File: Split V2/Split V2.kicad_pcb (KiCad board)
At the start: 2 copper layers, 170.2 x 121.3 mm, 75 parts, among them J1 AudioJack4

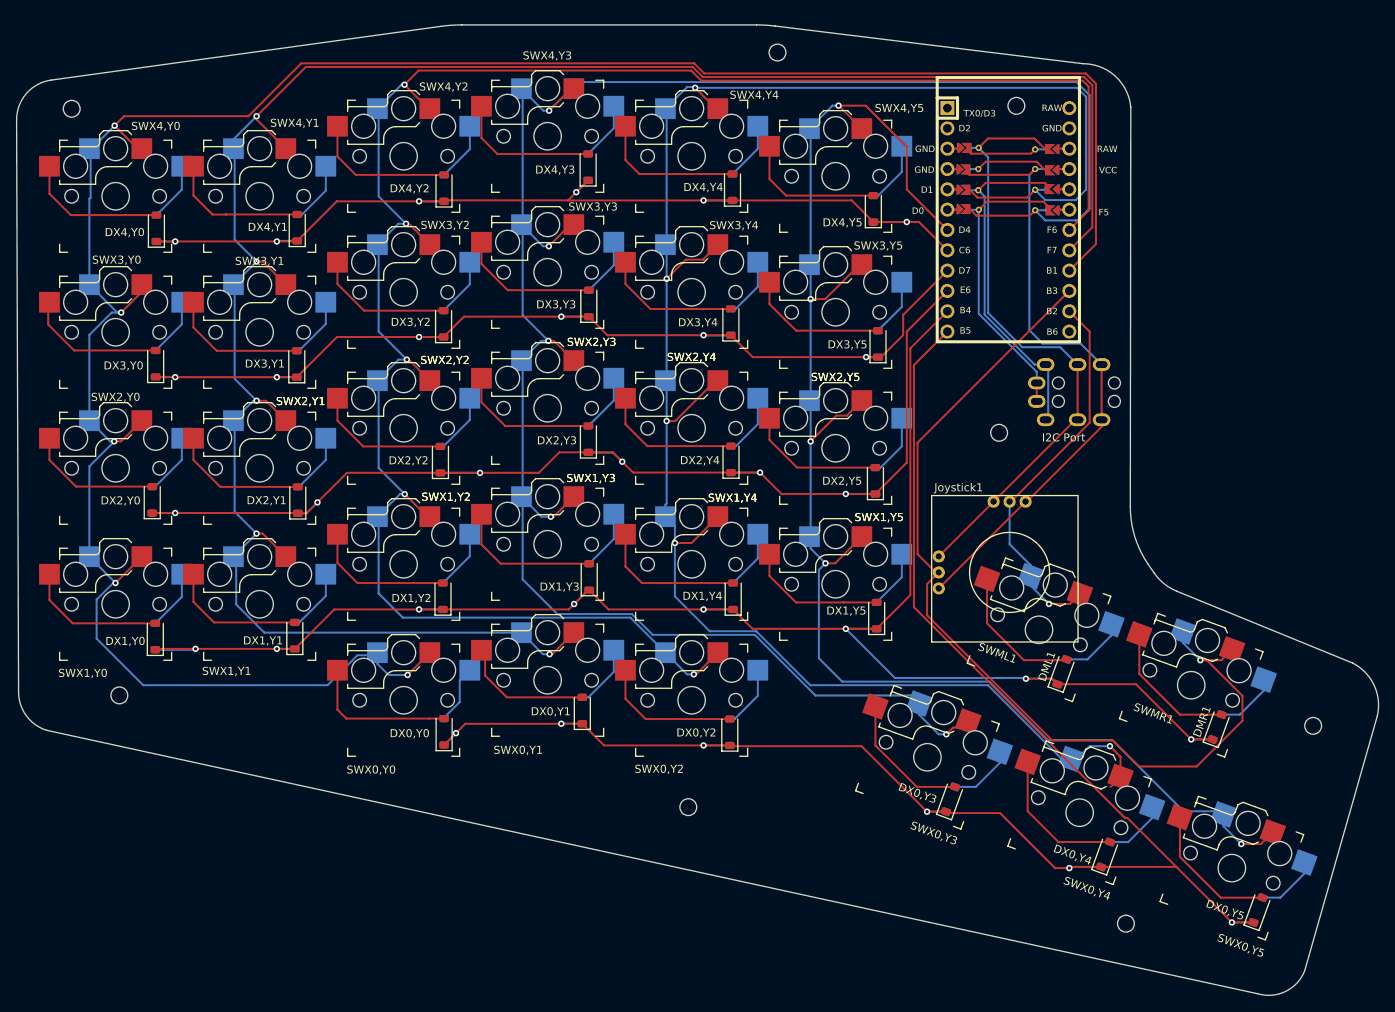
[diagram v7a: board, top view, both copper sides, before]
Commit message: Modified Split and made new
Modified the original split to correct ADC error for joystick and started work on a Split keyboard with cherry switches
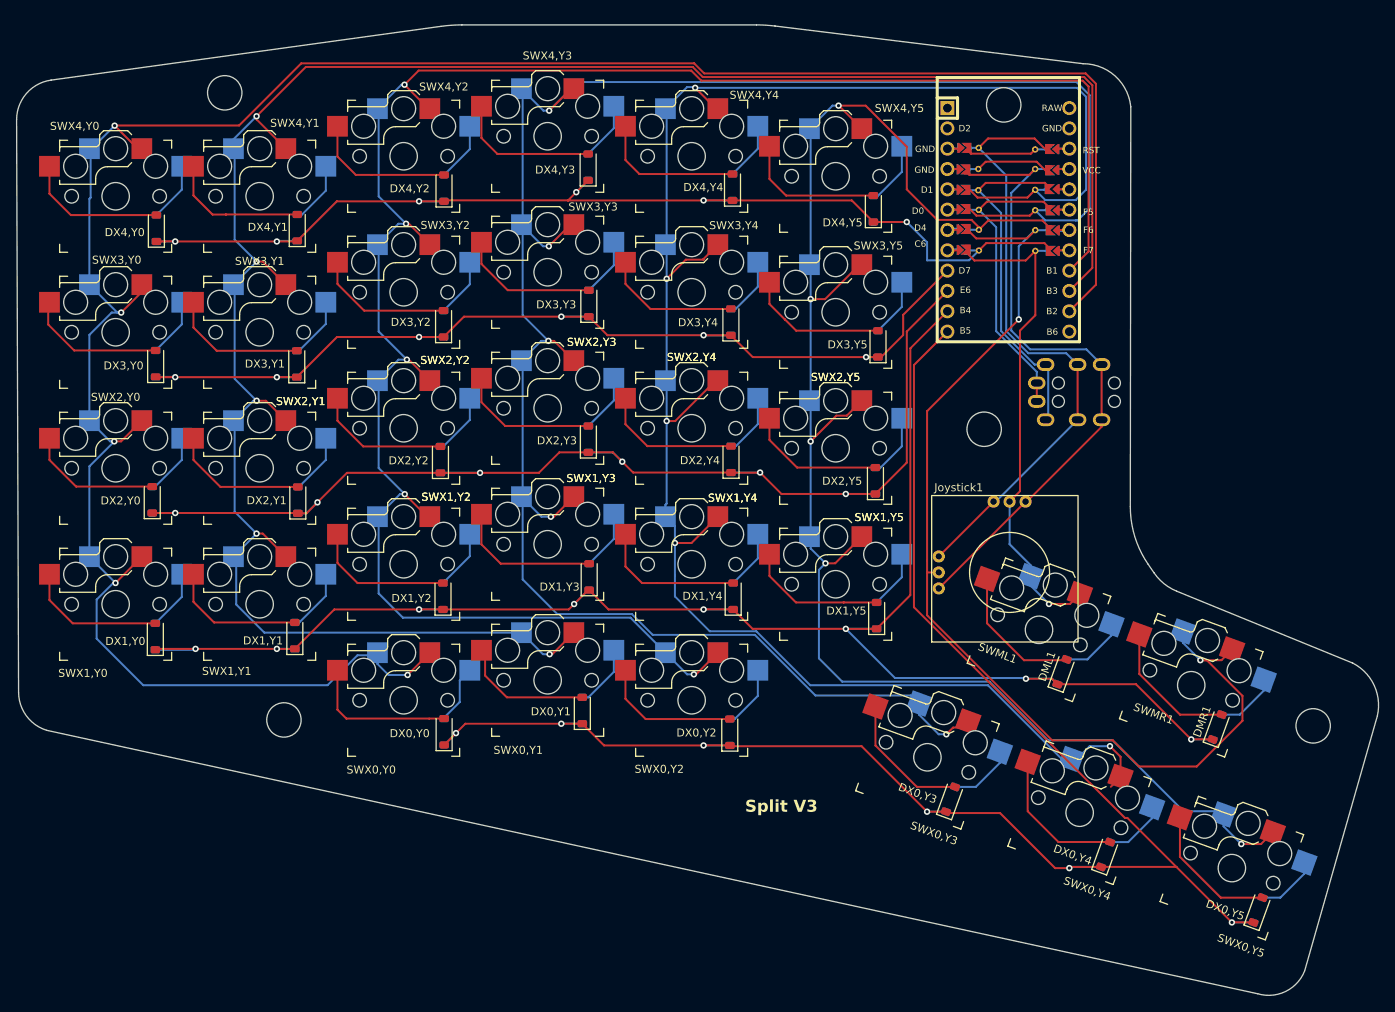
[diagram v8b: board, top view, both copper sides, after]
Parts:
- removed the REF** at (174.3, 58.1)
- removed the REF** at (217.9, 167.0)
- removed the REF** at (163.2, 152.4)
- REF** (x5): value MountingHole_2.1mm -> MountingHole_4.3mm_M4_ISO14580; footprint MountingHole:MountingHole_2.1mm -> MountingHole:MountingHole_4.3mm_M4_ISO14580
- moved REF** 20.8 mm to (112.6, 141.5)
- moved REF** 19.2 mm to (105.2, 63.1)
- moved REF** 1.93 mm to (200.2, 105.2)
- moved REF** 1.59 mm to (202.6, 64.6)
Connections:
- Joystick1 pad 2: B3 -> Joy1
- Joystick1 pad 3: B2 -> Joy2
- ProMicro1 pad 14: B2 -> Col0
- ProMicro1 pad 15: B3 -> Col1
- ProMicro1 pad 16: Col0 -> Col2
- ProMicro1 pad 17: Col1 -> Joy2
- ProMicro1 pad 18: Col2 -> Joy1
- SWML1 pad 1: B2 -> Joy2
- SWMR1 pad 1: B3 -> Joy1
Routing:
- net Joy1: track 0.00 -> 138.8 mm, vias 0 -> 2
- net B3: track 119.2 -> 0.00 mm, vias 1 -> 0
- net Joy2: track 0.00 -> 67.1 mm, vias 0 -> 1
- net B2: track 48.3 -> 0.00 mm, vias 1 -> 0
- net Row4: track 125.1 -> 145.3 mm
- net Col5: track 190.7 -> 208.9 mm
- net Col0: track 294.5 -> 299.6 mm
- net Col2: track 246.1 -> 251.2 mm
- net Col1: track 265.4 -> 270.5 mm
- net VCC: track 81.6 -> 84.8 mm
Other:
- board text added: "Split V3"
